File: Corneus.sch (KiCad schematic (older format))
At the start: 142 parts

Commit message: LED PWM
immediately thought of a schematic update to make: LED PWM
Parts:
- added Q?: Q_NPN_BCE, symbol Device:Q_NPN_BCE
- added R?: 1.5k, symbol Device:R_Small
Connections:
- net GND: now also Q?.3 (E)
- net LEDGND: now also Q?.2 (C)
- new net: Q?.1 (B), R?.1
- new net LEDPWM: R?.2
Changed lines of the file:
@@
 	1    0    0    -1
 $EndComp
+$Comp
+L Device:Q_NPN_BCE Q?
+U 1 1 5F5CD88C
+P 7450 4900
+F 0 "Q?" H 7641 4946 50  0000 L CNN
+F 1 "Q_NPN_BCE" H 7641 4855 50  0000 L CNN
+F 2 "" H 7650 5000 50  0001 C CNN
+F 3 "~" H 7450 4900 50  0001 C CNN
+	1    7450 4900
+	1    0    0    -1
+$EndComp
+$Comp
+L Device:R_Small R?
+U 1 1 5F5CF76A
+P 7150 4900
+F 0 "R?" V 6954 4900 50  0000 C CNN
+F 1 "1.5k" V 7045 4900 50  0000 C CNN
+F 2 "" H 7150 4900 50  0001 C CNN
+F 3 "~" H 7150 4900 50  0001 C CNN
+	1    7150 4900
+	0    1    1    0
+$EndComp
+Text GLabel 7050 4900 0    50   Input ~ 0
+LEDPWM
+$Comp
+L power:GND #PWR?
+U 1 1 5F5D128A
+P 7550 5100
+F 0 "#PWR?" H 7550 4850 50  0001 C CNN
+F 1 "GND" H 7555 4927 50  0000 C CNN
+F 2 "" H 7550 5100 50  0001 C CNN
+F 3 "" H 7550 5100 50  0001 C CNN
+	1    7550 5100
+	1    0    0    -1
+$EndComp
+Text GLabel 7550 4700 1    50   Input ~ 0
+LEDGND
 $EndSCHEMATC

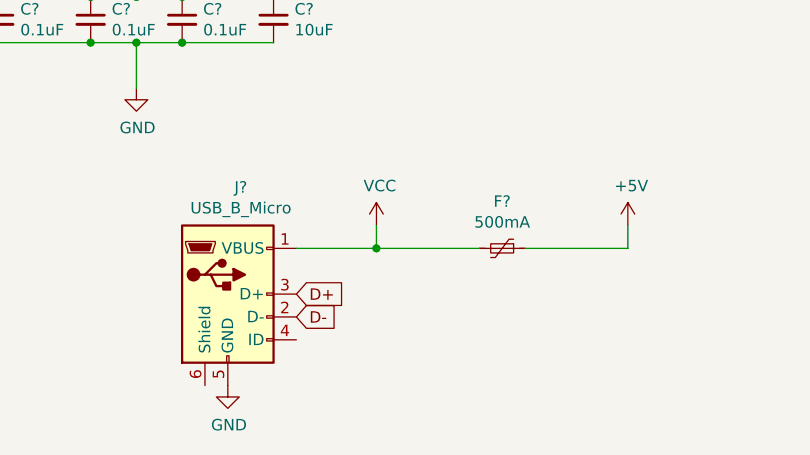
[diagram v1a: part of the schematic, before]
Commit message: USB resistors
another schematic update to add resistors to USB D+/-
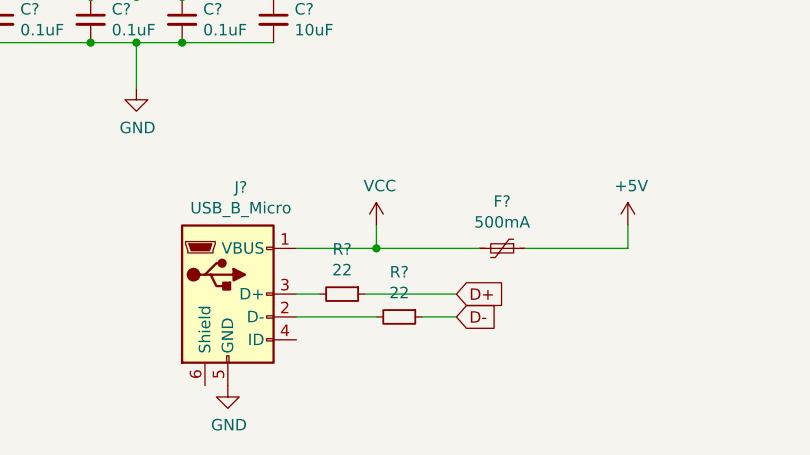
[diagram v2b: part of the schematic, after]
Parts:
- added R? (x2): 22, symbol Device:R_Small
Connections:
- net D+: now also R?.1; no longer J?.3 (D+)
- net D-: now also R?.1; no longer J?.2 (D-)
- new net: J?.2 (D-), R?.2
- new net: J?.3 (D+), R?.2
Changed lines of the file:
@@
 Wire Wire Line
 	2450 6750 2100 6750
-Text GLabel 2100 6950 2    50   Input ~ 0
+Text GLabel 2800 6950 2    50   Input ~ 0
 D+
-Text GLabel 2100 7050 2    50   Input ~ 0
+Text GLabel 2800 7050 2    50   Input ~ 0
 D-
 $Comp
@@
 Text GLabel 7550 4700 1    50   Input ~ 0
 LEDGND
+$Comp
+L Device:R_Small R?
+U 1 1 5F5EB1F7
+P 2300 6950
+F 0 "R?" V 2104 6950 50  0000 C CNN
+F 1 "22" V 2195 6950 50  0000 C CNN
+F 2 "" H 2300 6950 50  0001 C CNN
+F 3 "~" H 2300 6950 50  0001 C CNN
+	1    2300 6950
+	0    1    1    0
+$EndComp
+$Comp
+L Device:R_Small R?
+U 1 1 5F601D9F
+P 2550 7050
+F 0 "R?" V 2354 7050 50  0000 C CNN
+F 1 "22" V 2445 7050 50  0000 C CNN
+F 2 "" H 2550 7050 50  0001 C CNN
+F 3 "~" H 2550 7050 50  0001 C CNN
+	1    2550 7050
+	0    1    1    0
+$EndComp
+Wire Wire Line
+	2100 6950 2200 6950
+Wire Wire Line
+	2400 6950 2800 6950
+Wire Wire Line
+	2100 7050 2450 7050
+Wire Wire Line
+	2650 7050 2800 7050
 $EndSCHEMATC

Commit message: assigned reference designators
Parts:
- gave numbers to parts that had none: 140

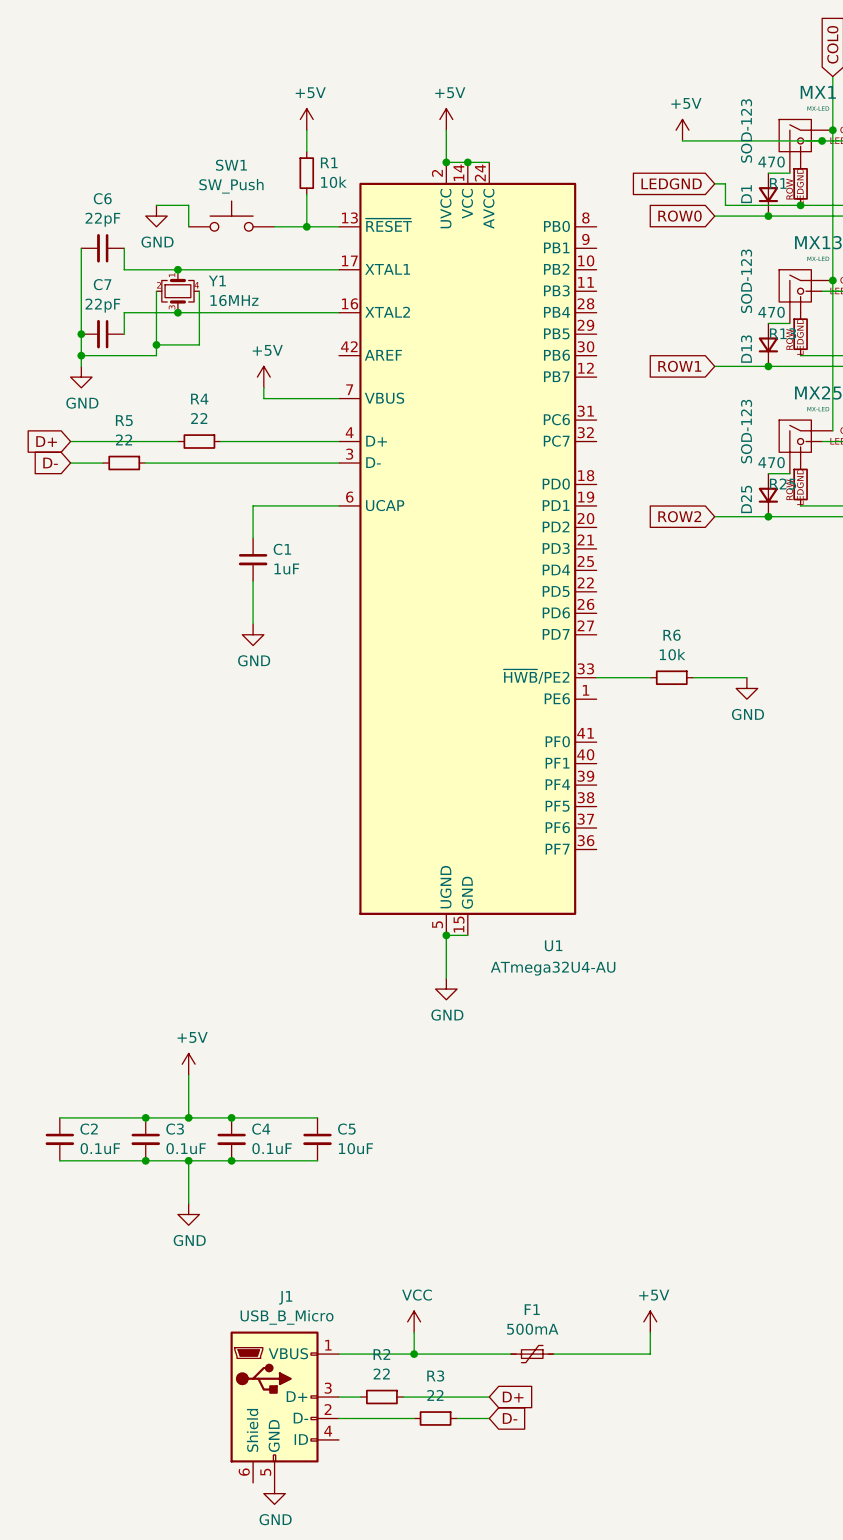
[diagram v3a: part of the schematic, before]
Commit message: add manufacturer USB footprint, renumber resistors
Realized I had R1-R6 but also my LED resistors were numbered in sync with the switches, so 1-6 were doubled up. Renumbered 1-6 to 43-48. Also, I found that the micro USB port manufacturer offers their own KiCAD footprint, so I added that.
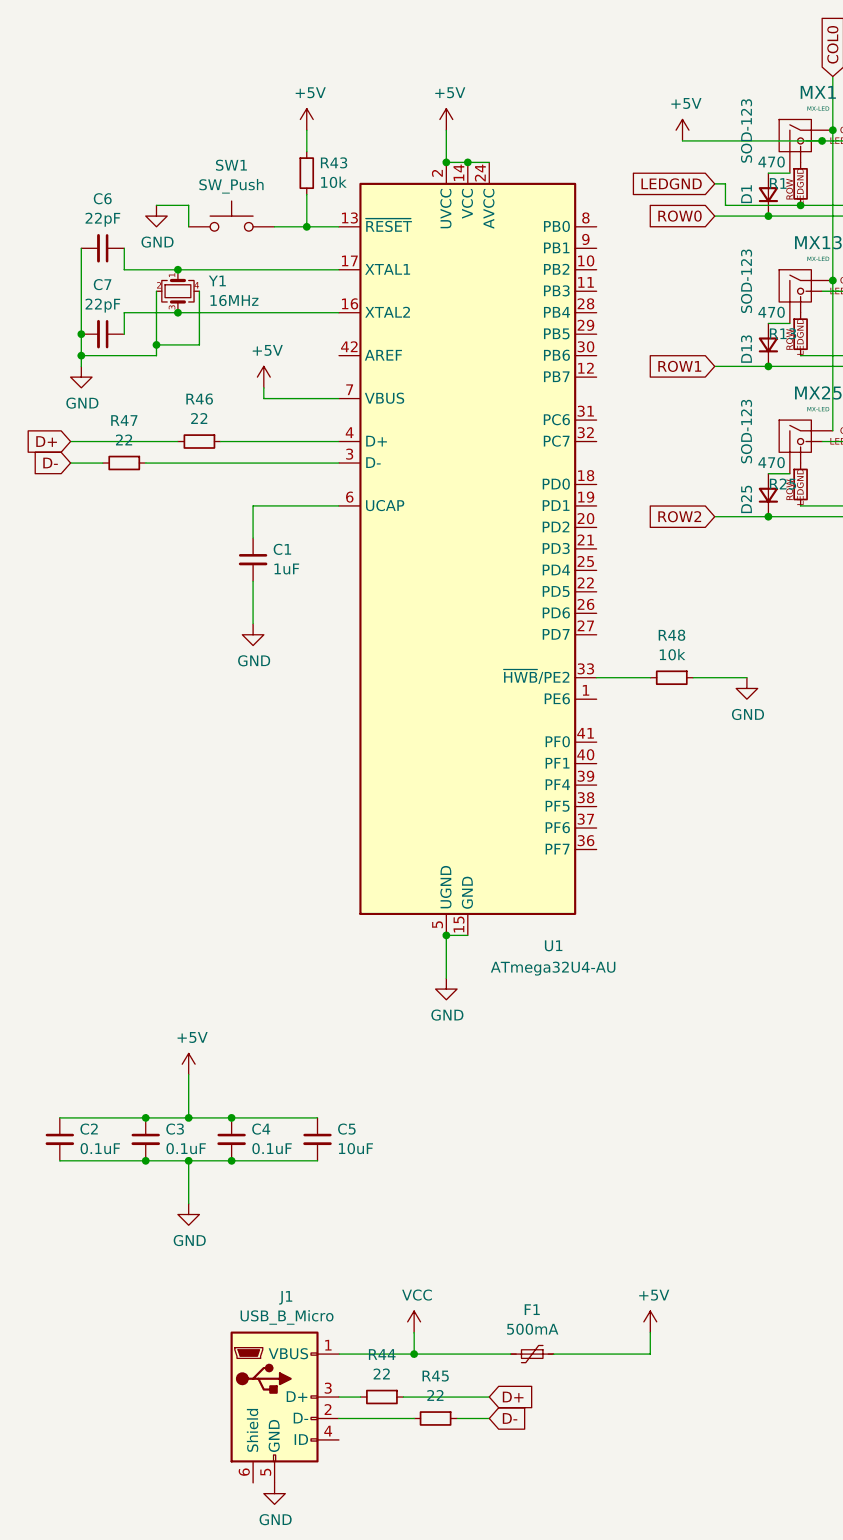
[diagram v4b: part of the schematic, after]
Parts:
- renumbered R1 to R43, R2 to R44, R3 to R45, R4 to R46, R5 to R47, R6 to R48
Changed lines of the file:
@@
 	2600 4800 2600 5000
 $Comp
-L Device:R_Small R6
+L Device:R_Small R48
 U 1 1 5EE95709
 P 3650 3600
-F 0 "R6" V 3454 3600 50  0000 C CNN
+F 0 "R48" V 3454 3600 50  0000 C CNN
 F 1 "10k" V 3545 3600 50  0000 C CNN
 F 2 "" H 3650 3600 50  0001 C CNN
@@
 	3300 3600 3550 3600
 $Comp
-L Device:R_Small R4
+L Device:R_Small R46
 U 1 1 5EE97B55
 P 1450 2500
-F 0 "R4" V 1254 2500 50  0000 C CNN
+F 0 "R46" V 1254 2500 50  0000 C CNN
 F 1 "22" V 1345 2500 50  0000 C CNN
 F 2 "" H 1450 2500 50  0001 C CNN
@@
 $EndComp
 $Comp
-L Device:R_Small R5
+L Device:R_Small R47
 U 1 1 5EE98301
 P 1100 2600
-F 0 "R5" V 904 2600 50  0000 C CNN
+F 0 "R47" V 904 2600 50  0000 C CNN
 F 1 "22" V 995 2600 50  0000 C CNN
 F 2 "" H 1100 2600 50  0001 C CNN
@@
 $EndComp
 $Comp
-L Device:R_Small R1
+L Device:R_Small R43
 U 1 1 5EEC55CA
 P 1950 1250
-F 0 "R1" H 2009 1296 50  0000 L CNN
+F 0 "R43" H 2009 1296 50  0000 L CNN
 F 1 "10k" H 2009 1205 50  0000 L CNN
 F 2 "" H 1950 1250 50  0001 C CNN
@@
 LEDGND
 $Comp
-L Device:R_Small R2
+L Device:R_Small R44
 U 1 1 5F5EB1F7
 P 2300 6950
-F 0 "R2" V 2104 6950 50  0000 C CNN
+F 0 "R44" V 2104 6950 50  0000 C CNN
 F 1 "22" V 2195 6950 50  0000 C CNN
 F 2 "" H 2300 6950 50  0001 C CNN
@@
 $EndComp
 $Comp
-L Device:R_Small R3
+L Device:R_Small R45
 U 1 1 5F601D9F
 P 2550 7050
-F 0 "R3" V 2354 7050 50  0000 C CNN
+F 0 "R45" V 2354 7050 50  0000 C CNN
 F 1 "22" V 2445 7050 50  0000 C CNN
 F 2 "" H 2550 7050 50  0001 C CNN
